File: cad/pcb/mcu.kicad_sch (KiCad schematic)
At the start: 5 parts

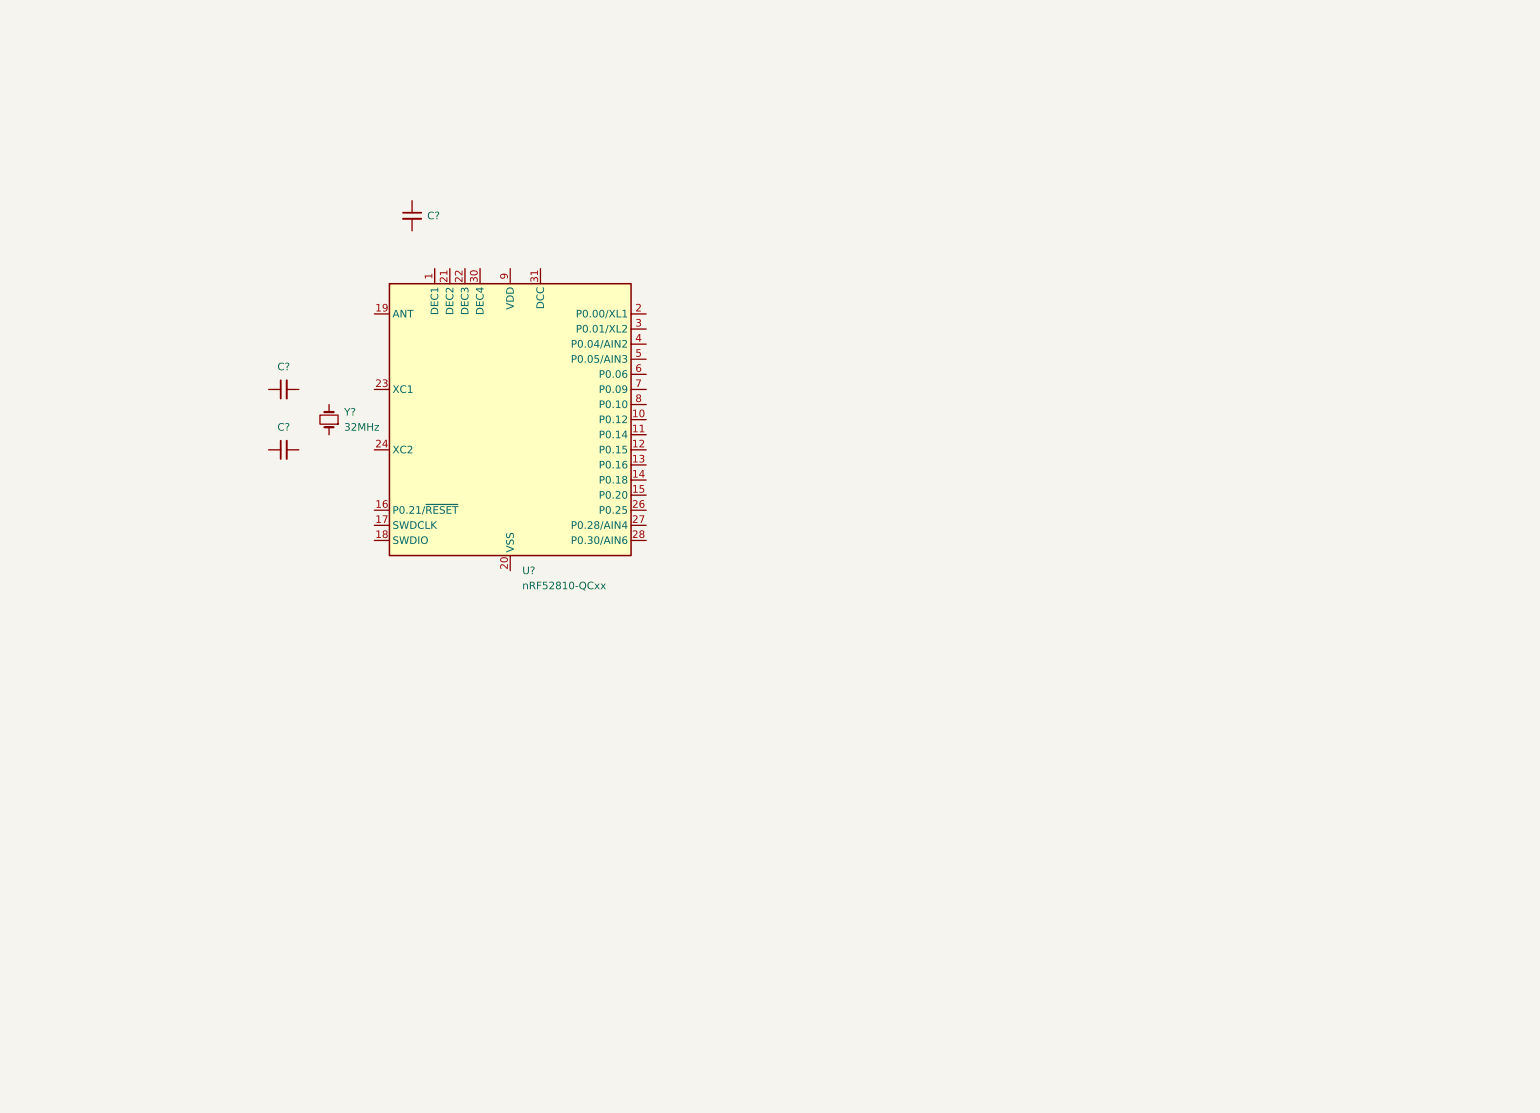
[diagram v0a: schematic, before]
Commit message: finish overview schematic page
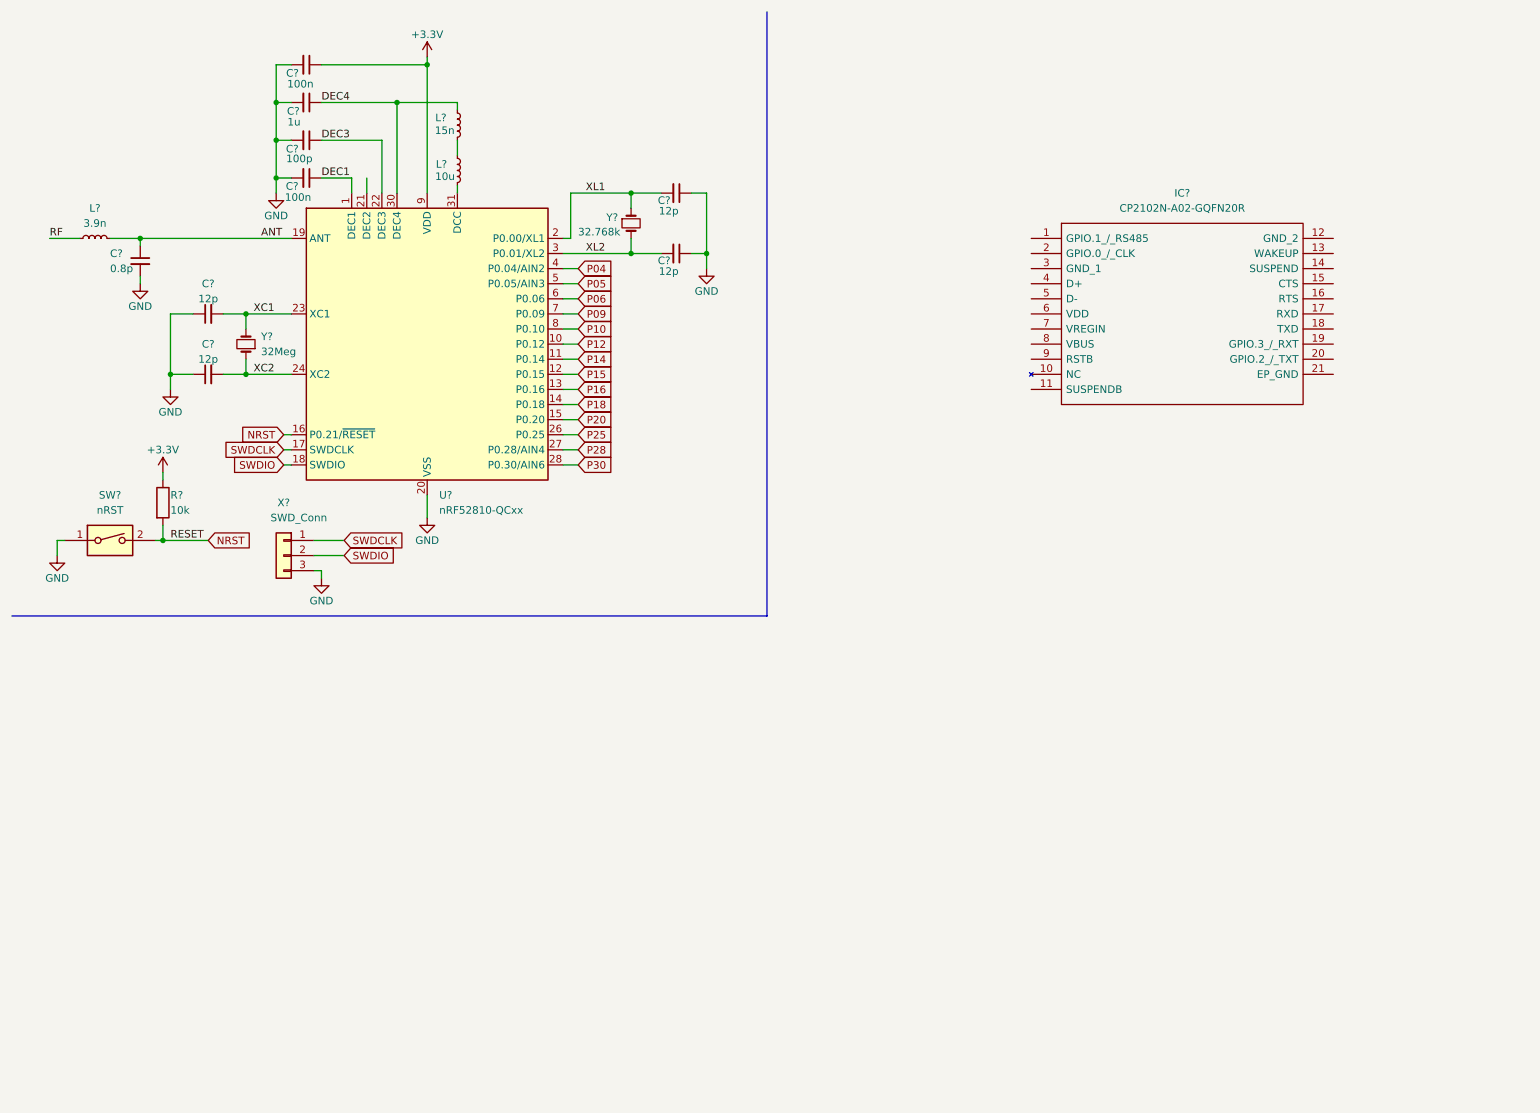
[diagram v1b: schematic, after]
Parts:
- added C? (x2): 12p, symbol Device:C_Small
- added C?: 1u, symbol Device:C_Small
- added C?: 100p, symbol Device:C_Small
- added C?: 100n, symbol Device:C_Small
- added C?: 0.8p, symbol Device:C_Small
- added IC?: CP2102N-A02-GQFN20R, CP2102NA02GQFN20, symbol USB-UART Bridge:CP2102N-A02-GQFN20R
- added L?: 15n, symbol Device:L_Small
- added L?: 3.9n, symbol Device:L_Small
- added L?: 10u, symbol Device:L_Small
- added R?: 10k, symbol Device:R
- added SW?: nRST, symbol Switch:SW_DIP_x01
- added X?: SWD_Conn, symbol Connector_Generic:Conn_01x03
- added Y?: 32.768k, symbol Device:Crystal_Small
- C? (x2): value C_Small -> 12p
- C?: value C_Small -> 100n
- Y?: value 32MHz -> 32Meg
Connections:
- net GND: now reaches C?.1
- net GND: now also C?.1, C?.2, U?.20 (VSS), U?.29 (VSS), U?.33 (VSS), C?.1, C?.1, C?.2, C?.2, C?.2, C?.2, SW?.1, X?.3 (Pin_3)
- net XC1: now reaches C?.2
- net XC1: now also U?.23 (XC1), Y?.2
- net DEC1: now reaches U?.1 (DEC1)
- net DEC1: now also C?.1
- net P12: now reaches U?.10 (P0.12)
- net P14: now reaches U?.11 (P0.14)
- net P15: now reaches U?.12 (P0.15)
- net P16: now reaches U?.13 (P0.16)
- net P18: now reaches U?.14 (P0.18)
- net P20: now reaches U?.15 (P0.20)
- net NRST: now reaches U?.16 (P0.21/~{RESET})
- net NRST: now also R?.2, SW?.2
- net SWDCLK: now reaches U?.17 (SWDCLK)
- net SWDCLK: now also X?.1 (Pin_1)
- net SWDIO: now reaches U?.18 (SWDIO)
- net SWDIO: now also X?.2 (Pin_2)
- net ANT: now reaches U?.19 (ANT)
- net ANT: now also C?.1, L?.2
- net XL1: now reaches U?.2 (P0.00/XL1)
- net XL1: now also C?.2, Y?.1
- net DEC3: now reaches U?.22 (DEC3)
- net DEC3: now also C?.1
- net XC2: now reaches U?.24 (XC2)
- net XC2: now also C?.2, Y?.1
- net +3V3: now reaches U?.25 (VDD), U?.32 (VDD), U?.9 (VDD)
- net +3V3: now also C?.1, R?.1
- net P25: now reaches U?.26 (P0.25)
- net P28: now reaches U?.27 (P0.28/AIN4)
- net P30: now reaches U?.28 (P0.30/AIN6)
- net XL2: now reaches U?.3 (P0.01/XL2)
- net XL2: now also C?.2, Y?.2
- net DEC4: now reaches U?.30 (DEC4)
- net DEC4: now also C?.1, L?.2
- net at U?.31 (DCC): now also L?.1
- net P04: now reaches U?.4 (P0.04/AIN2)
- net P05: now reaches U?.5 (P0.05/AIN3)
- net P06: now reaches U?.6 (P0.06)
- net P09: now reaches U?.7 (P0.09)
- net P10: now reaches U?.8 (P0.10)
- new net: L?.1, L?.2
- new net RF: L?.1
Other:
- moved on the sheet: C?, U?, Y?

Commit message: finish mcu connections
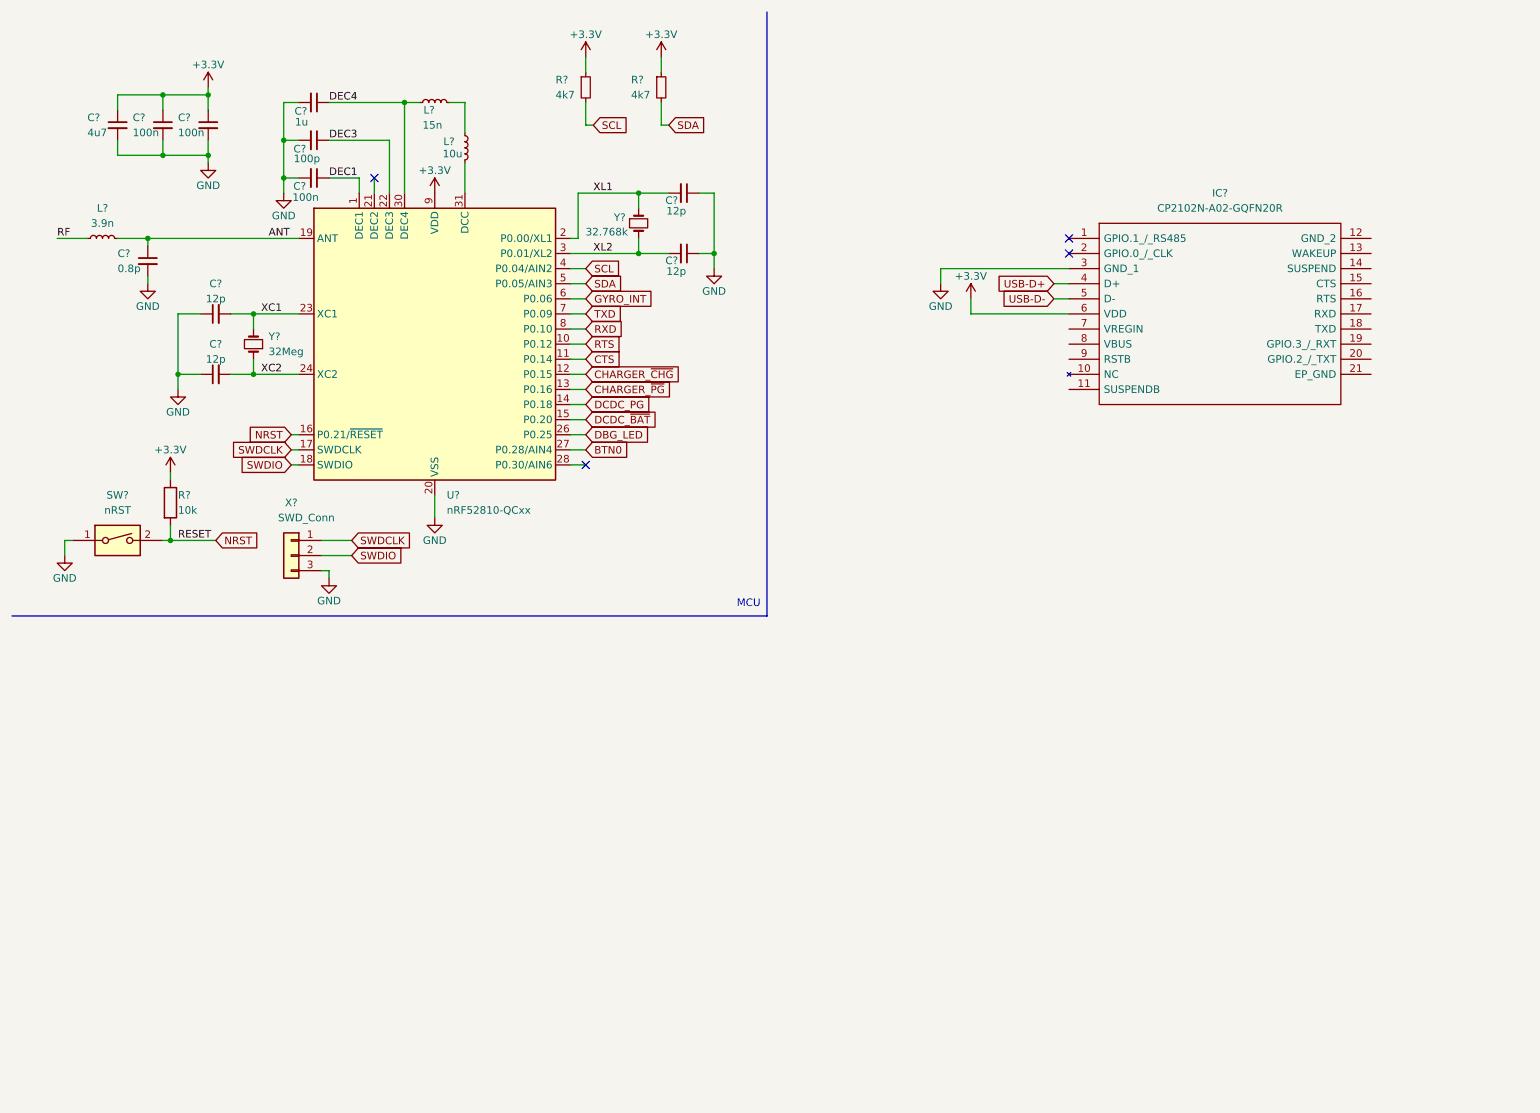
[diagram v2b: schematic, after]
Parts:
- removed C?: 100n, symbol Device:C_Small
- added C?: 4u7, symbol Device:C_Small
- added C? (x2): 100n, symbol Device:C_Small
- added R? (x2): 4k7, symbol Device:R_Small
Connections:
- net +3V3: now also IC?.6 (VDD), C?.1, C?.1, C?.1, R?.1, R?.1
- net GND: now also IC?.3 (GND_1), C?.2, C?.2, C?.2
- net USB-D+: now reaches IC?.4 (D+)
- net USB-D-: now reaches IC?.5 (D-)
- net P04 renamed SCL
- net SCL: now also R?.2
- net P05 renamed SDA
- net SDA: now also R?.2
- net P06 renamed GYRO_INT
- net P09 renamed TXD
- net P10 renamed RXD
- net P12 renamed RTS
- net P14 renamed CTS
- net P15 renamed CHARGER_~{CHG}
- net P16 renamed CHARGER_~{PG}
- net P18 renamed DCDC_PG
- net P20 renamed DCDC_~{BAT}
- net P25 renamed DBG_LED
- net P28 renamed BTN0
- net P30: no longer names the net of U?.28 (P0.30/AIN6)
- no-connect marks 0 -> 4
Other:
- note added: "MCU"
- moved on the sheet: C?, IC?, L?, R?, SW?, U?, X?, Y?

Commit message: changed MCU package
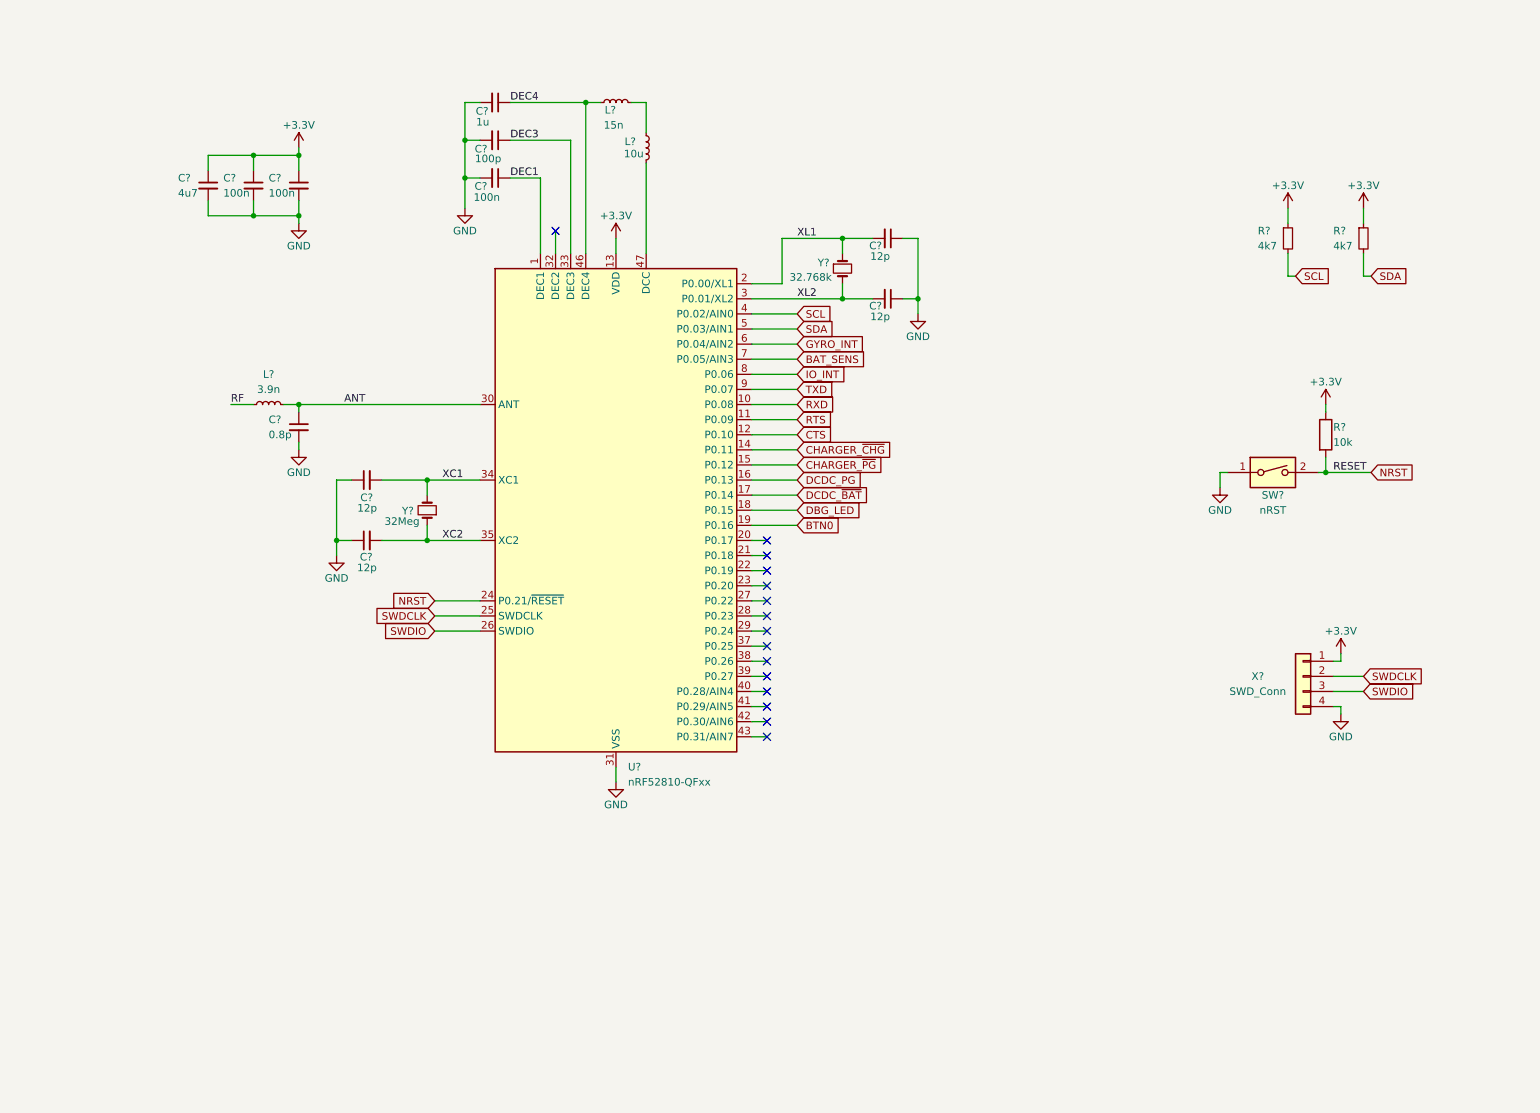
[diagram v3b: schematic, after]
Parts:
- removed IC?: CP2102N-A02-GQFN20R, CP2102NA02GQFN20, symbol USB-UART Bridge:CP2102N-A02-GQFN20R
- removed U?: nRF52810-QCxx, Package_DFN_QFN:QFN-32-1EP_5x5mm_P0.5mm_EP3.6x3.6mm, symbol MCU_Nordic:nRF52810-QCxx
- removed X?: SWD_Conn, symbol Connector_Generic:Conn_01x03
- added U?: nRF52810-QFxx, Package_DFN_QFN:QFN-48-1EP_6x6mm_P0.4mm_EP4.6x4.6mm, symbol MCU_Nordic:nRF52810-QFxx
- added X?: SWD_Conn, symbol Connector_Generic:Conn_01x04
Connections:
- net +3V3: now also U?.13 (VDD), U?.36 (VDD), U?.48 (VDD), X?.1 (Pin_1)
- net ANT: now also U?.30 (ANT)
- net BTN0: now also U?.19 (P0.16)
- net CHARGER_~{CHG}: now also U?.14 (P0.11)
- net CHARGER_~{PG}: now also U?.15 (P0.12)
- net CTS: now also U?.12 (P0.10)
- net DBG_LED: now also U?.18 (P0.15)
- net DCDC_PG: now also U?.16 (P0.13)
- net DCDC_~{BAT}: now also U?.17 (P0.14)
- net DEC1: now also U?.1 (DEC1)
- net DEC3: now also U?.33 (DEC3)
- net DEC4: now also U?.46 (DEC4)
- net GND: now also U?.31 (VSS), U?.45 (VSS), U?.49 (VSS), X?.4 (Pin_4)
- net GYRO_INT: now also U?.6 (P0.04/AIN2)
- net NRST: now also U?.24 (P0.21/~{RESET})
- net RTS: now also U?.11 (P0.09)
- net RXD: now also U?.10 (P0.08)
- net SCL: now also U?.4 (P0.02/AIN0)
- net SDA: now also U?.5 (P0.03/AIN1)
- net SWDCLK: now also U?.25 (SWDCLK), X?.2 (Pin_2)
- net SWDIO: now also U?.26 (SWDIO), X?.3 (Pin_3)
- net TXD: now also U?.9 (P0.07)
- net XC1: now also U?.34 (XC1)
- net XC2: now also U?.35 (XC2)
- net XL1: now also U?.2 (P0.00/XL1)
- net XL2: now also U?.3 (P0.01/XL2)
- net at L?.1: now also U?.47 (DCC)
- new net BAT_SENS: U?.7 (P0.05/AIN3)
- new net IO_INT: U?.8 (P0.06)
- no-connect marks 4 -> 15
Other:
- note removed: "MCU"
- moved on the sheet: C?, L?, R?, SW?, Y?

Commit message: add charging & preotection circuit
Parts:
- gave numbers to parts that had none: 22
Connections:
- net DCC: now reaches L5.1, U1.47 (DCC)
